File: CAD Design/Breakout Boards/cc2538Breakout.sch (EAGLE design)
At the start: 11 parts

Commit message: cc2538 breakout
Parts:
- added C3, C4: 47pF, PCB 3.0.0:DISCRETE_CC0402
- added C5, C6: .1uF, PCB 3.0.0:DISCRETE_CC0402
- added JP1: USB-MICROB, SparkFun-Connectors:USB-MICROB
- added R3: 56k, PCB 3.0.0:RCL_R-US_R0402
- added R4, R5: 33, PCB 3.0.0:RCL_R-US_R0402
- added U$3: STELLARIS_LAUNCHPAD_EM_HEADERS, AustinBlackstoneEngineeringPublic:STELLARIS_LAUNCHPAD_EM_HEADERS
- added VREG1: VOLTAGE-REGULATORS_LM3940IMP, PCB 3.0.0:VOLTAGE-REGULATORS_LM3940IMP
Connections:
- new net N$12: U$1.PA7
- new net N$15: U$1.PA6
- new net N$16: U$1.PA5
- new net N$17: U$1.PA4
- new net N$18: U$1.PA3
- new net N$19: U$1.PA2
- new net N$21: U$1.PA0
- new net N$22: U$1.PB0
- new net N$23: U$1.PC7
- new net N$24: U$1.PC6
- new net N$25: U$1.PC5
- new net N$26: U$1.PC4
- new net N$27: U$1.PC3
- new net N$28: U$1.PC2
- new net N$29: U$1.PC1
- new net N$3: U$1.PD5
- new net N$30: R3.1, U$1.PC0
- new net N$31: U$1.PB1
- new net N$32: U$1.PB2
- new net N$33: U$1.PB3
- new net N$34: U$1.PB4
- new net N$35: U$1.PB5
- new net N$36: U$1.PB6
- new net N$37: U$1.PB7
- new net N$38: R5.1, U$1.USB_P
- new net N$39: U$1.JTAG_TCK
- new net N$4: U$1.PD4
- new net N$40: U$1.JTAG_TMS
- new net N$41: C3.1, JP1.D-, R4.2
- new net N$42: C4.2, JP1.D+, R3.2, R5.2
- new net N$43: R4.1, U$1.USB_N
- new net N$44: R2.1
- new net N$45: C6.2, JP1.VBUS, VREG1.IN
- new net N$7: U$1.PD2
- new net N$8: U$1.PD1
- new net N$9: U$1.PD0
- net GND: now also C3.2, C4.1, C5.2, C6.1, JP1.GND, U$1.PD6/XOSC32K_Q1, U$1.PD7/XOSC32K_Q2, U$4.6, VREG1.GND; no longer R2.1
- net VCC: now also C5.1, VREG1.OUT
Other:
- moved on the sheet: C1, C2, U$4, XTAL-32MHZ

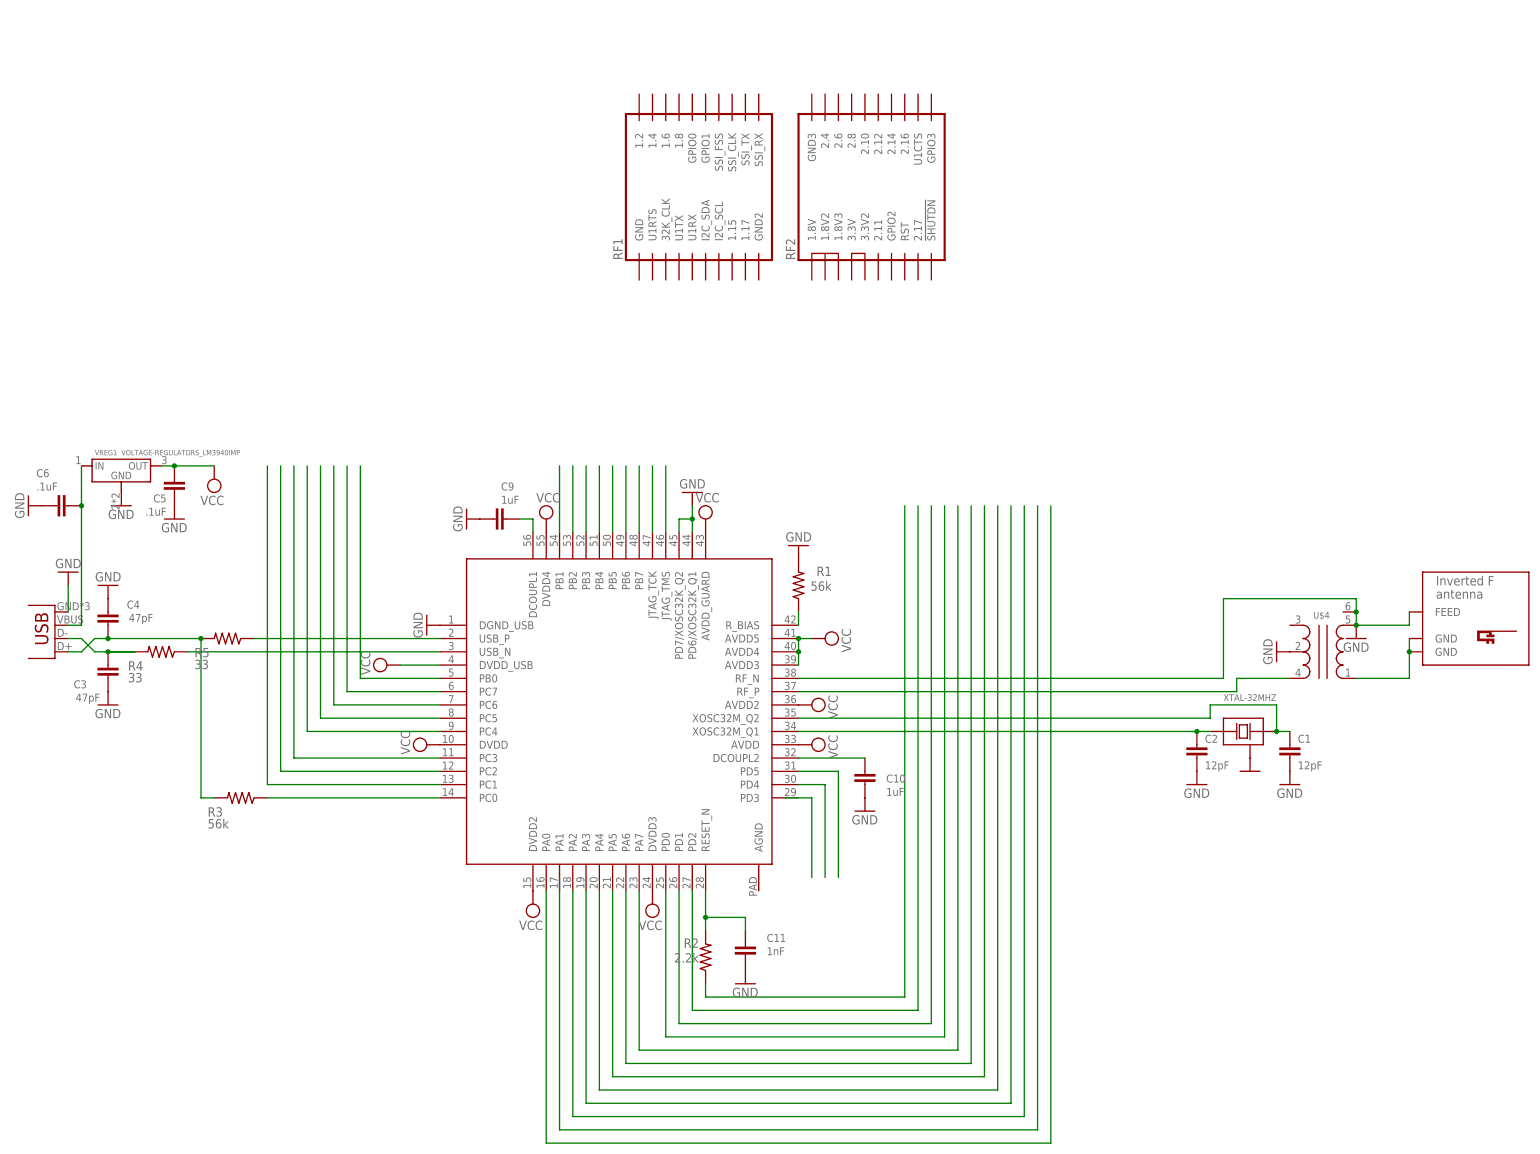
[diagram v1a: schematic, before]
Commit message: cc2538EM schematic finished
Pin matched headers, added VCC decoupling bank.  Ready for board layout.
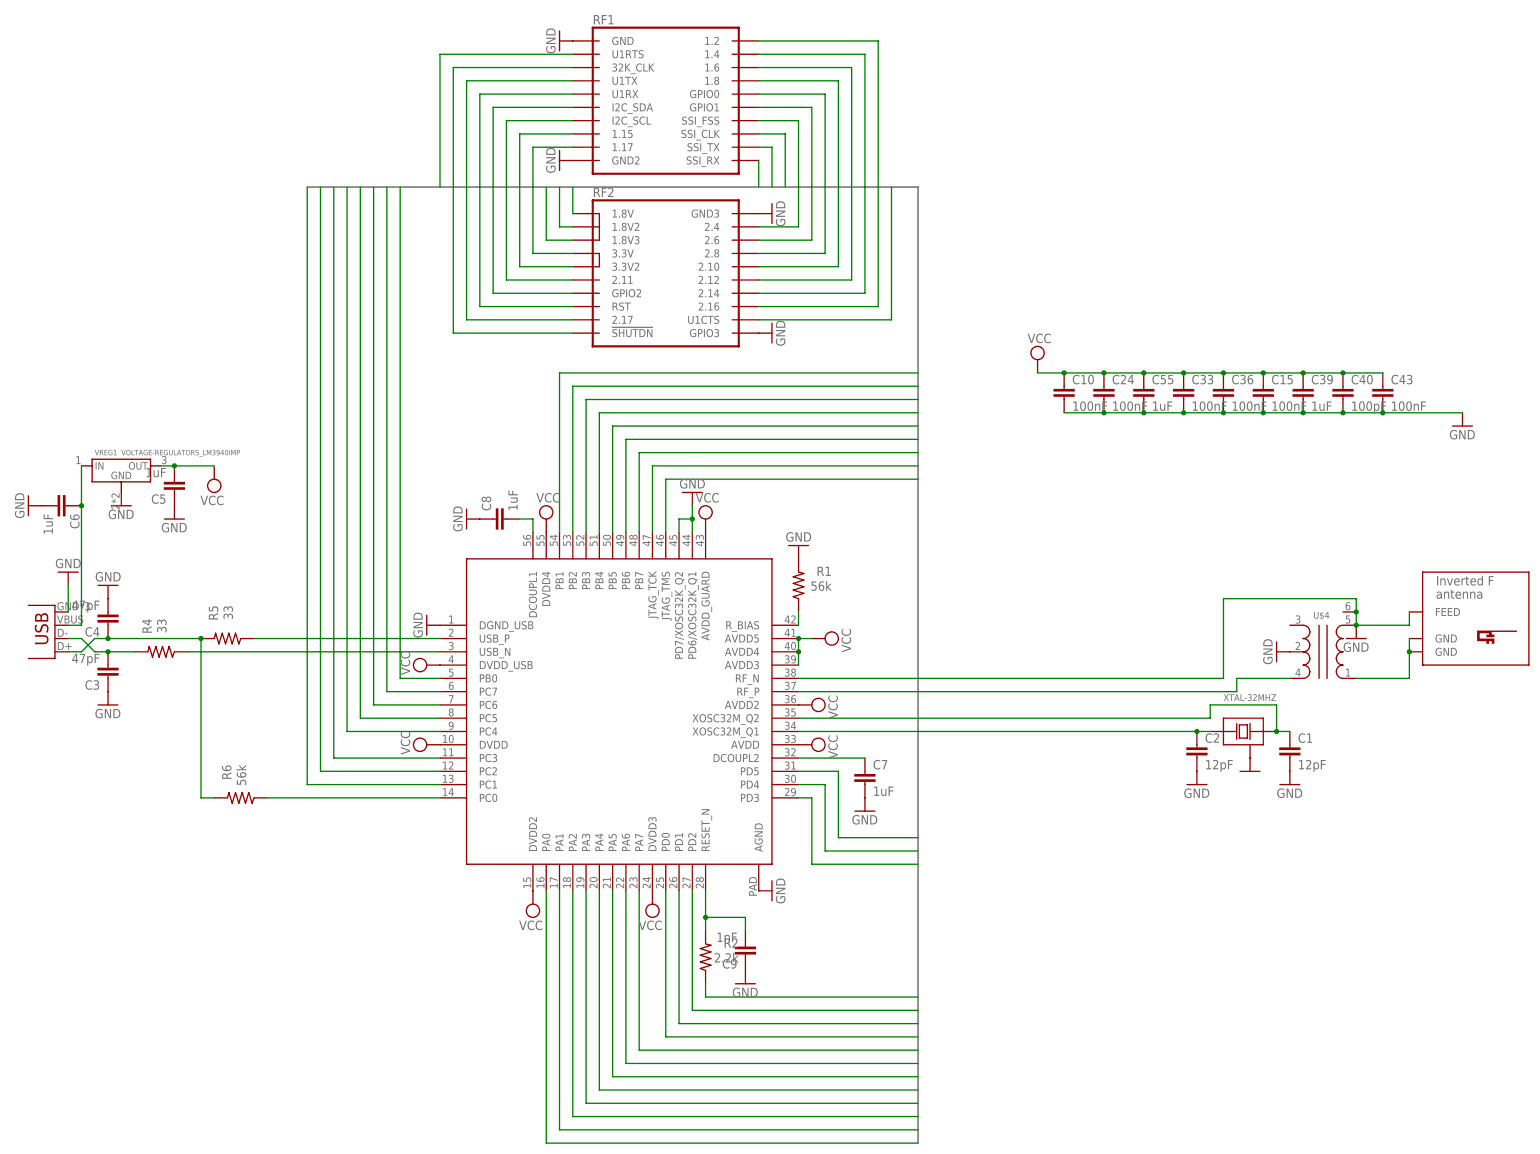
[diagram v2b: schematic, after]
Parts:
- removed C11: 1nF, PCB 3.0.0:DISCRETE_CC0402
- removed R3: 56k, PCB 3.0.0:RCL_R-US_R0402
- added C15, C24, C33, C36, C43: 100nF, resistor:C-EUC0805
- added C39, C55, C7, C8: 1uF, resistor:C-EUC0805
- added C40: 100pF, resistor:C-EUC0805
- added R6: 56k, resistor:R-US_R0805
- C1, C2, C3, C4: device PCB 3.0.0:DISCRETE_CC0402 -> resistor:C-EUC0805
- C10: value 1uF -> 100nF; device PCB 3.0.0:DISCRETE_CC0402 -> resistor:C-EUC0805
- C5, C6: value .1uF -> 1uF; device PCB 3.0.0:DISCRETE_CC0402 -> resistor:C-EUC0805
- C9: value 1uF -> 1nF; device PCB 3.0.0:DISCRETE_CC0402 -> resistor:C-EUC0805
- R1, R2, R4, R5: device PCB 3.0.0:RCL_R-US_R0402 -> resistor:R-US_R0805
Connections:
- removed net N$12: U$1.PA7
- removed net N$15: U$1.PA6
- removed net N$16: U$1.PA5
- removed net N$17: U$1.PA4
- removed net N$18: U$1.PA3
- removed net N$19: U$1.PA2
- removed net N$21: U$1.PA0
- removed net N$22: U$1.PB0
- removed net N$23: U$1.PC7
- removed net N$24: U$1.PC6
- removed net N$25: U$1.PC5
- removed net N$26: U$1.PC4
- removed net N$27: U$1.PC3
- removed net N$28: U$1.PC2
- removed net N$29: U$1.PC1
- removed net N$3: U$1.PD5
- removed net N$31: U$1.PB1
- removed net N$32: U$1.PB2
- removed net N$33: U$1.PB3
- removed net N$34: U$1.PB4
- removed net N$35: U$1.PB5
- removed net N$36: U$1.PB6
- removed net N$37: U$1.PB7
- removed net N$39: U$1.JTAG_TCK
- removed net N$4: U$1.PD4
- removed net N$40: U$1.JTAG_TMS
- removed net N$44: R2.1
- removed net N$7: U$1.PD2
- removed net N$8: U$1.PD1
- removed net N$9: U$1.PD0
- new net I/O10: U$1.PC6, U$3.GPIO0
- new net I/O11: U$1.PB2, U$3.I2C_SDA
- new net I/O12: U$1.PC7, U$3.GPIO1
- new net I/O13: U$1.PB3, U$3.I2C_SCL
- new net I/O14: U$1.PA3, U$3.SSI_FSS
- new net I/O15: U$1.PB4, U$3.1.15
- new net I/O16: U$1.PA2, U$3.SSI_CLK
- new net I/O17: U$1.PB5, U$3.1.17
- new net I/O18: U$1.PA4, U$3.SSI_TX
- new net I/O2: U$1.PC2, U$3.1.2
- new net I/O20: U$1.PA5, U$3.SSI_RX
- new net I/O21: U$1.JTAG_TCK, U$3.1.8V
- new net I/O23: U$3.1.8V2
- new net I/O24: U$1.JTAG_TMS, U$3.2.4
- new net I/O25: U$1.PA6, U$3.1.8V3
- new net I/O26: U$1.PA7, U$3.2.6
- new net I/O27: U$3.3.3V
- new net I/O28: U$1.PD4, U$3.2.8
- new net I/O29: U$3.3.3V2
- new net I/O3: U$1.PB0, U$3.U1RTS
- new net I/O30: U$1.PD5, U$3.2.10
- new net I/O31: U$1.PC1, U$3.2.11
- new net I/O32: U$1.PD0, U$3.2.12
- new net I/O33: U$3.GPIO2
- new net I/O34: U$1.PD1, U$3.2.14
- new net I/O35: R2.1, U$3.RST
- new net I/O36: U$1.PD2, U$3.2.16
- new net I/O37: U$1.PB6, U$3.2.17
- new net I/O38: U$1.PD3, U$3.U1CTS
- new net I/O39: U$1.PB7, U$3.!SHUTDN
- new net I/O4: U$1.PC3, U$3.1.4
- new net I/O5: U$1.PB1, U$3.32K_CLK
- new net I/O6: U$1.PC4, U$3.1.6
- new net I/O7: U$1.PA0, U$3.U1TX
- new net I/O8: U$1.PC5, U$3.1.8
- new net I/O9: U$1.PA1, U$3.U1RX
- net GND: now also C15.2, C24.2, C3.1, C33.2, C36.2, C39.2, C4.2, C40.2, C43.2, C5.1, C55.2, C6.2, C7.2, C8.1, C9.1, U$1.AGND, U$3.GND, U$3.GND2, U$3.GND3, U$3.GPIO3; no longer C11.2, C3.2, C4.1, C5.2, C6.1, C9.2
- net N$10: now also C8.2; no longer C9.1
- net N$11: now also C7.1; no longer C10.1
- net N$14: now also C9.2; no longer C11.1
- net N$30: now also R6.1; no longer R3.1
- net N$41: now also C3.2; no longer C3.1
- net N$42: now also C4.1, R6.2; no longer C4.2, R3.2
- net N$45: now also C6.1; no longer C6.2
- net VCC: now also C10.1, C15.1, C24.1, C33.1, C36.1, C39.1, C40.1, C43.1, C5.2, C55.1; no longer C5.1
